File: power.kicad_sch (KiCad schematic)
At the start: 36 parts, among them K1 G6K-2F-Y-TR, K2 G6K-2F-Y-TR, K3 G6K-2F-Y-TR, K4 G6K-2F-Y-TR, Q1 DMN2056U, Q2 DMN2056U, Q3 DMN2056U, Q4 DMN2056U, U2 TPS7A2401DBVR, U3 PI4IOE5V9536UEX

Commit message: Board is fully routed
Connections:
- net RELAY3: now reaches D5.2 (A), K4.1 (COIL1), Q4.3 (D)
- net RELAY1: now reaches D3.2 (A), K2.1 (COIL1), Q2.3 (D)
- net RELAY0: now reaches D2.2 (A), K1.1 (COIL1), Q1.3 (D)
- net RELAY2: now reaches D4.2 (A), K3.1 (COIL1), Q3.3 (D)
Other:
- moved on the sheet: D2, D3, D4, D5, K1C, K2C, K3C, K4C

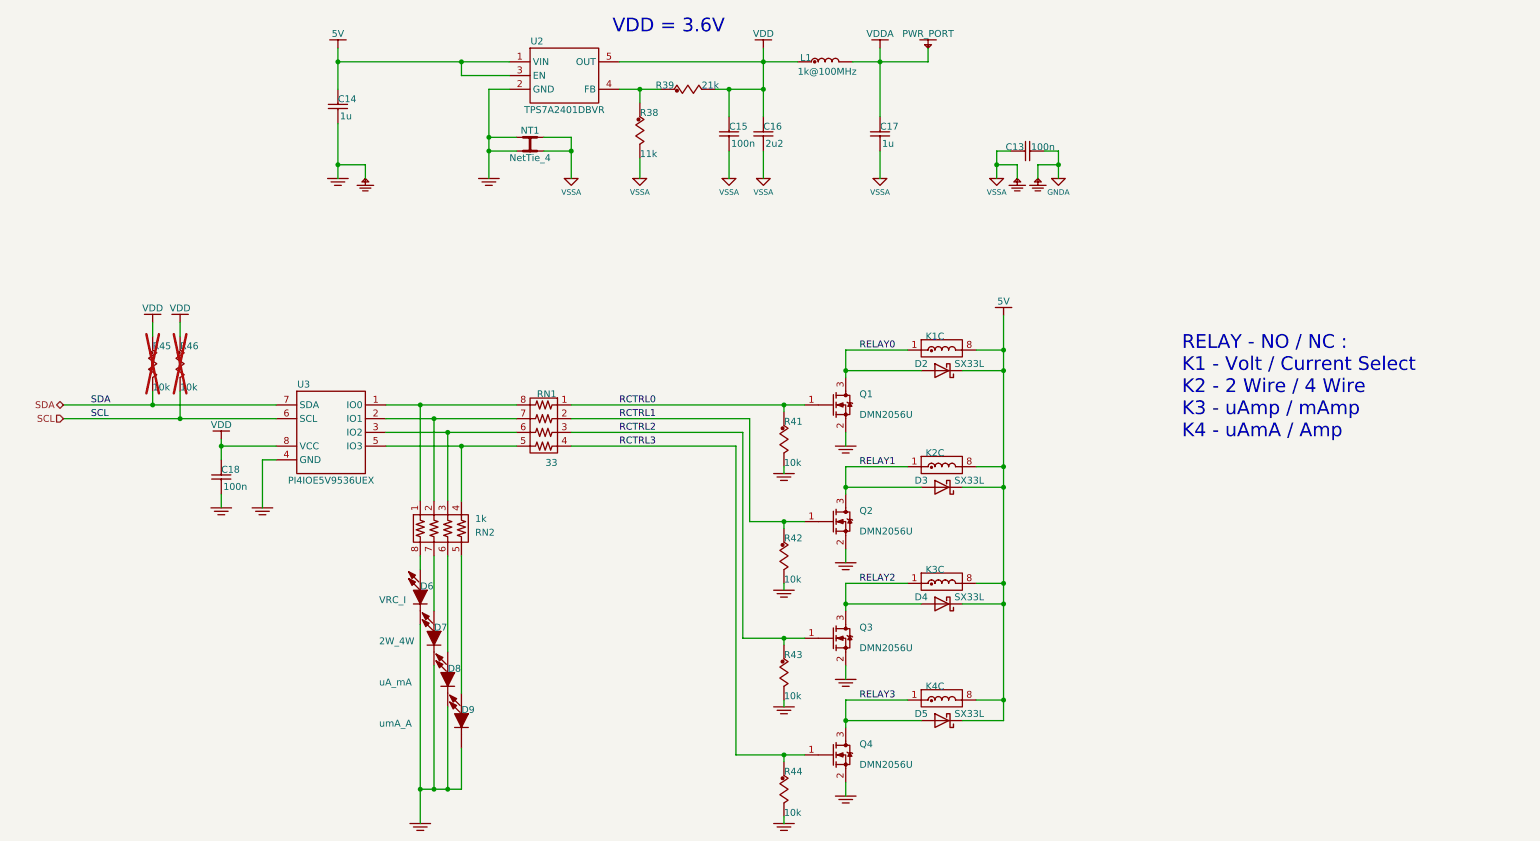
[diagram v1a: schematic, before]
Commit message: Added galvanic isolation
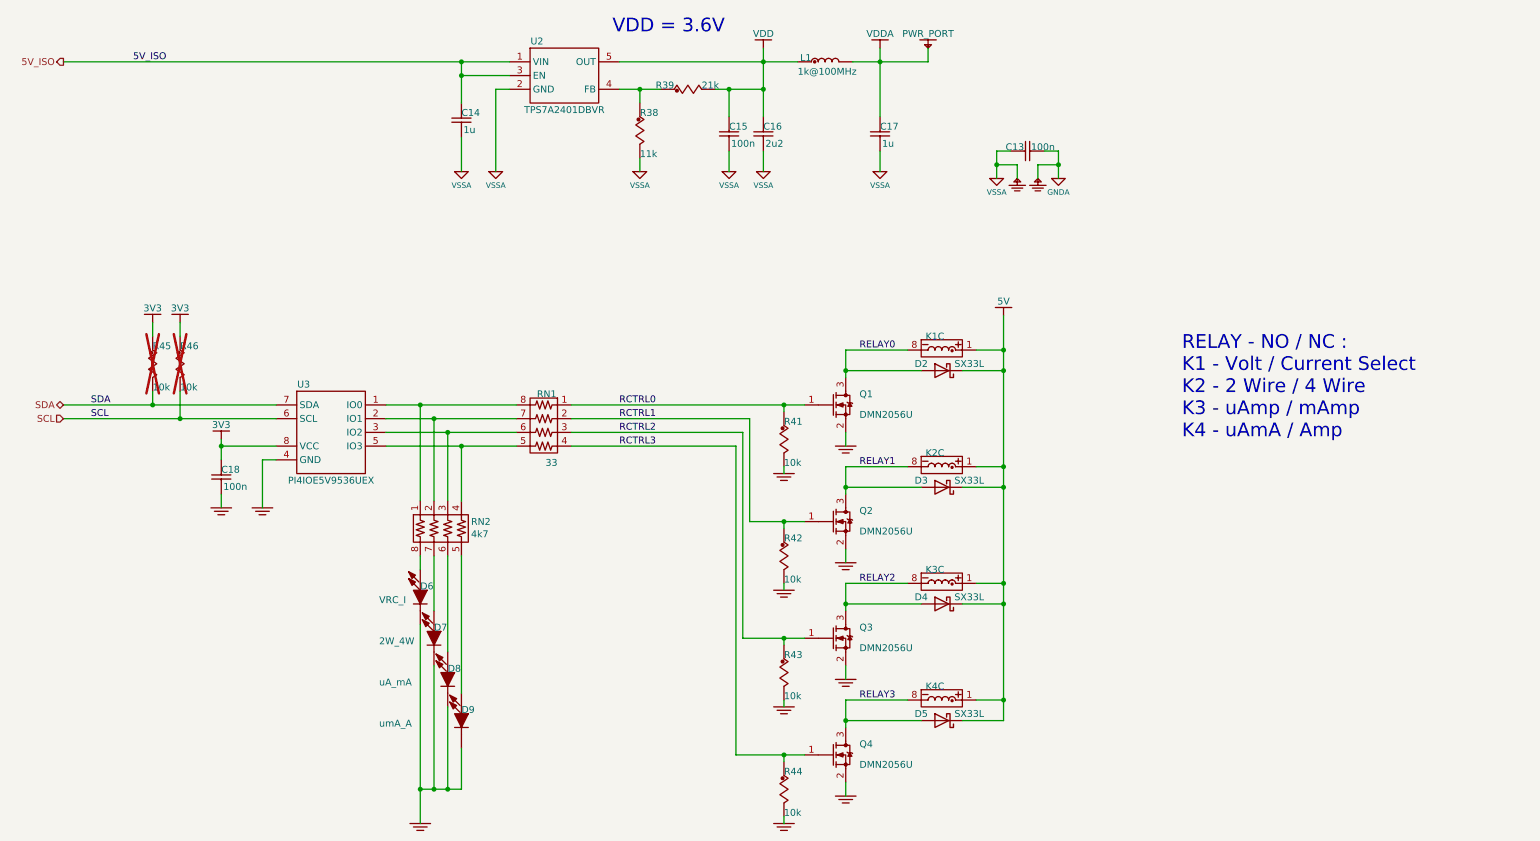
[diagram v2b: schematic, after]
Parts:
- removed NT1: NetTie_4, NetTie:NetTie-4_SMD_Pad2.0mm, symbol Device:NetTie_4
- removed RN2: 1k, Resistor_SMD:R_Array_Convex_4x0603, symbol sesa_resistor:1k_4a_0603
- added RN2: 4k7, Resistor_SMD:R_Array_Convex_4x0603, symbol sesa_resistor:4k7_4a_0603
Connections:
- net 5V: now also K1.1 (COIL1), K2.1 (COIL1), K3.1 (COIL1), K4.1 (COIL1); no longer C14.2, K1.8 (COIL2), K2.8 (COIL2), K3.8 (COIL2), K4.8 (COIL2), U2.1 (VIN), U2.3 (EN)
- net GND: no longer C14.1, U2.2 (GND)
- net RELAY0: now also K1.8 (COIL2); no longer K1.1 (COIL1)
- net RELAY1: now also K2.8 (COIL2); no longer K2.1 (COIL1)
- net RELAY2: now also K3.8 (COIL2); no longer K3.1 (COIL1)
- net RELAY3: now also K4.8 (COIL2); no longer K4.1 (COIL1)
- net VDD: no longer C18.2, R45.1, R46.1, U3.8 (VCC)
- net VSSA: now also C14.1, U2.2 (GND)
- net at D7.2 (A): now also RN2.7
- net at RN1.5, U3.5 (IO3): now also RN2.4
- net at RN1.6, U3.3 (IO2): now also RN2.3
- net at RN1.7, U3.2 (IO1): now also RN2.2
- net at RN1.8, U3.1 (IO0): now also RN2.1
- net at D8.2 (A): now also RN2.6
- net at D9.2 (A): now also RN2.5
- net at D6.2 (A): now also RN2.8
- new net 3V3: C18.2, R45.1, R46.1, U3.8 (VCC)
- new net 5V_ISO: C14.2, U2.1 (VIN), U2.3 (EN)
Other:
- moved on the sheet: C14

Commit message: Schematics updated with current protection and EEPROM
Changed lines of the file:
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@@
 	)
 	(symbol
-		(lib_id "sesa_old:GND")
+		(lib_id "sesa_power:GND")
 		(at 58.42 115.57 0)
 		(unit 1)
@@
 			(effects
 				(font
-					(size 1.524 1.524)
+					(size 1.27 1.27)
 				)
-				(hide yes)
 			)
 		)
@@
 			(effects
 				(font
-					(size 1.524 1.524)
+					(size 1.27 1.27)
 				)
-				(hide yes)
 			)
 		)
@@
 			)
 		)
-		(property "Description" ""
+		(property "Description" "Led smd 0603, green"
 			(at 97.79 139.7 0)
 			(effects
@@
 			)
 		)
-		(property "Description" ""
+		(property "Description" "resistor, 0603, 125 mW"
 			(at 162.56 162.56 0)
 			(effects
@@
 			)
 		)
-		(property "Description" ""
+		(property "Description" "resistor, 0603, 100 mW, 1%"
 			(at 139.7 38.1 0)
 			(effects
@@
 			)
 		)
-		(property "Description" ""
+		(property "Description" " MOSFET N-CHANNEL 20V, Vgss +/-8V, Vgs(th) 1V, Id 4A"
 			(at 171.45 161.29 0)
 			(effects
@@
 	)
 	(symbol
-		(lib_id "sesa_old:GND")
+		(lib_id "sesa_power:GND")
 		(at 66.04 115.57 0)
 		(unit 1)
@@
 			(effects
 				(font
-					(size 1.524 1.524)
+					(size 1.27 1.27)
 				)
-				(hide yes)
 			)
 		)
@@
 			(effects
 				(font
-					(size 1.524 1.524)
+					(size 1.27 1.27)
 				)
-				(hide yes)
 			)
 		)
@@
 	)
 	(symbol
-		(lib_id "sesa_old:GND")
+		(lib_id "sesa_power:GND")
 		(at 173.99 125.73 0)
 		(unit 1)
@@
 			(effects
 				(font
-					(size 1.524 1.524)
+					(size 1.27 1.27)
 				)
-				(hide yes)
 			)
 		)
@@
 			(effects
 				(font
-					(size 1.524 1.524)
+					(size 1.27 1.27)
 				)
-				(hide yes)
 			)
 		)
@@
 			)
 		)
-		(property "Description" ""
+		(property "Description" "resistor, 0603, 125 mW"
 			(at 162.56 119.38 0)
 			(effects
@@
 			)
 		)
-		(property "Description" ""
+		(property "Description" "DIODE SCHOTTKY 20V 1A SOD123FL"
 			(at 191.77 111.76 0)
 			(effects
@@
 			)
 		)
-		(property "Description" ""
+		(property "Description" "8 resistor network, star topology, bussed resistors, small US symbol"
 			(at 120.65 105.41 0)
 			(effects
@@
 			)
 		)
-		(property "Description" ""
+		(property "Description" "DIODE SCHOTTKY 20V 1A SOD123FL"
 			(at 191.77 90.17 0)
 			(effects
@@
 	)
 	(symbol
-		(lib_id "sesa_old:GND")
+		(lib_id "sesa_power:GND")
 		(at 162.56 173.99 0)
 		(unit 1)
@@
 			(effects
 				(font
-					(size 1.524 1.524)
+					(size 1.27 1.27)
 				)
-				(hide yes)
 			)
 		)
@@
 			(effects
 				(font
-					(size 1.524 1.524)
+					(size 1.27 1.27)
 				)
-				(hide yes)
 			)
 		)
@@
 	)
 	(symbol
-		(lib_id "sesa_old:GND")
+		(lib_id "sesa_power:GND")
 		(at 95.25 173.99 0)
 		(unit 1)
@@
 			(effects
 				(font
-					(size 1.524 1.524)
+					(size 1.27 1.27)
 				)
-				(hide yes)
 			)
 		)
@@
 			(effects
 				(font
-					(size 1.524 1.524)
+					(size 1.27 1.27)
 				)
-				(hide yes)
 			)
 		)
@@
 	)
 	(symbol
-		(lib_id "sesa_old:GND")
+		(lib_id "sesa_power:GND")
 		(at 173.99 104.14 0)
 		(unit 1)
@@
 			(effects
 				(font
-					(size 1.524 1.524)
+					(size 1.27 1.27)
 				)
-				(hide yes)
 			)
 		)
@@
 			(effects
 				(font
-					(size 1.524 1.524)
+					(size 1.27 1.27)
 				)
-				(hide yes)
 			)
 		)
@@
 			)
 		)
-		(property "Description" ""
+		(property "Description" "non polar capacitor, 0603 case"
 			(at 152.4 49.53 0)
 			(effects
@@
 			)
 		)
-		(property "Description" ""
+		(property "Description" "non polar capacitor, 0603 case"
 			(at 58.42 113.03 0)
 			(effects
@@
 			)
 		)
-		(property "Description" ""
+		(property "Description" "LDO Voltage Regulators 200-mA, 18-V, ultra-low-IQ, low-dropout (LDO) voltage regulator with enable 5-SOT-23 -40 to 125"
 			(at 115.57 40.64 0)
 			(effects
@@
 			)
 		)
-		(property "Description" ""
+		(property "Description" "Led smd 0603, green"
 			(at 100.33 147.32 0)
 			(effects
@@
 	)
 	(symbol
-		(lib_id "sesa_old:GND")
+		(lib_id "sesa_power:GND")
 		(at 173.99 168.91 0)
 		(unit 1)
@@
 			(effects
 				(font
-					(size 1.524 1.524)
+					(size 1.27 1.27)
 				)
-				(hide yes)
 			)
 		)
@@
 			(effects
 				(font
-					(size 1.524 1.524)
+					(size 1.27 1.27)
 				)
-				(hide yes)
 			)
 		)
@@
 			)
 		)
-		(property "Description" ""
+		(property "Description" "resistor, 0603, 125 mW"
 			(at 50.8 83.82 0)
 			(effects
@@
 			)
 		)
-		(property "Description" ""
+		(property "Description" "resistor, 0603, 125 mW"
 			(at 45.72 83.82 0)
 			(effects
@@
 	)
 	(symbol
-		(lib_id "sesa_old:GND")
+		(lib_id "sesa_power:GND")
 		(at 173.99 147.32 0)
 		(unit 1)
@@
 			(effects
 				(font
-					(size 1.524 1.524)
+					(size 1.27 1.27)
 				)
-				(hide yes)
 			)
 		)
@@
 			(effects
 				(font
-					(size 1.524 1.524)
+					(size 1.27 1.27)
 				)
-				(hide yes)
 			)
 		)
@@
 	)
 	(symbol
-		(lib_id "sesa_old:GND")
+		(lib_id "sesa_power:GND")
 		(at 162.56 130.81 0)
 		(unit 1)
@@
 			(effects
 				(font
-					(size 1.524 1.524)
+					(size 1.27 1.27)
 				)
-				(hide yes)
 			)
 		)
@@
 			(effects
 				(font
-					(size 1.524 1.524)
+					(size 1.27 1.27)
 				)
-				(hide yes)
 			)
 		)
@@
 			)
 		)
-		(property "Description" ""
+		(property "Description" "resistor, 0603, 100 mW"
 			(at 135.89 40.64 0)
 			(effects
@@
 			)
 		)
-		(property "Description" ""
+		(property "Description" "resistor, 0603, 125 mW"
 			(at 162.56 140.97 0)
 			(effects
@@
 			)
 		)
-		(property "Description" ""
+		(property "Description" "Led smd 0603, green"
 			(at 95.25 132.08 0)
 			(effects
@@
 			)
 		)
-		(property "Description" ""
+		(property "Description" " MOSFET N-CHANNEL 20V, Vgss +/-8V, Vgs(th) 1V, Id 4A"
 			(at 171.45 139.7 0)
 			(effects
@@
 			)
 		)
-		(property "Description" ""
+		(property "Description" "Led smd 0603, green"
 			(at 102.87 154.94 0)
 			(effects
@@
 			)
 		)
-		(property "Description" ""
+		(property "Description" " MOSFET N-CHANNEL 20V, Vgss +/-8V, Vgs(th) 1V, Id 4A"
 			(at 171.45 118.11 0)
 			(effects
@@
 	)
 	(symbol
-		(lib_id "sesa_old:GND")
+		(lib_id "sesa_power:GND")
 		(at 162.56 109.22 0)
 		(unit 1)
@@
 			(effects
 				(font
-					(size 1.524 1.524)
+					(size 1.27 1.27)
 				)
-				(hide yes)
 			)
 		)
@@
 			(effects
 				(font
-					(size 1.524 1.524)
+					(size 1.27 1.27)
 				)
-				(hide yes)
 			)
 		)
@@
 	)
 	(symbol
-		(lib_id "sesa_old:GND")
+		(lib_id "sesa_power:GND")
 		(at 162.56 152.4 0)
 		(unit 1)
@@
 			(effects
 				(font
-					(size 1.524 1.524)
+					(size 1.27 1.27)
 				)
-				(hide yes)
 			)
 		)
@@
 			(effects
 				(font
-					(size 1.524 1.524)
+					(size 1.27 1.27)
 				)
-				(hide yes)
 			)
 		)
@@
 			)
 		)
-		(property "Description" ""
+		(property "Description" "DIODE SCHOTTKY 20V 1A SOD123FL"
 			(at 191.77 133.35 0)
 			(effects
@@
 			)
 		)
-		(property "Description" ""
+		(property "Description" "Inductor"
 			(at 165.1 33.02 0)
 			(effects
@@
 			)
 		)
-		(property "Description" ""
+		(property "Description" "DIODE SCHOTTKY 20V 1A SOD123FL"
 			(at 191.77 154.94 0)
 			(effects
@@
 			)
 		)
-		(property "Description" ""
+		(property "Description" "non polar capacitor, 0603 case"
 			(at 180.34 49.53 0)
 			(effects
@@
 			)
 		)
-		(property "Description" ""
+		(property "Description" "non polar capacitor, 0603 case"
 			(at 210.82 49.53 0)
 			(effects
@@
 			)
 		)
-		(property "Description" ""
+		(property "Description" "non polar capacitor, 0603 case"
 			(at 102.87 46.99 0)
 			(effects
@@
 			)
 		)
-		(property "Description" ""
+		(property "Description" "non polar capacitor, 0603 case"
 			(at 158.75 49.53 0)
 			(effects
@@
 			)
 		)
-		(property "Description" ""
+		(property "Description" " MOSFET N-CHANNEL 20V, Vgss +/-8V, Vgs(th) 1V, Id 4A"
 			(at 171.45 96.52 0)
 			(effects
@@
 			)
 		)
-		(property "Description" ""
+		(property "Description" "resistor, 0603, 125 mW"
 			(at 162.56 97.79 0)
 			(effects

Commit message: Isolated analog path is fully routed
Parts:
- D8: value uA_mA -> mA_uA
- D9: value umA_A -> A_umA
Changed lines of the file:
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@@
 			)
 		)
-		(property "Value" "uA_mA"
+		(property "Value" "mA_uA"
 			(at 87.63 148.59 0)
 			(effects
@@
 			)
 		)
-		(property "Value" "umA_A"
+		(property "Value" "A_umA"
 			(at 87.63 156.21 0)
 			(effects
